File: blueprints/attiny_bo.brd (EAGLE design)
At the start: 35.8 x 20 mm, 8 parts, among them IC1 ATTiny85, J1 AVR_SPI_PRG_6NS

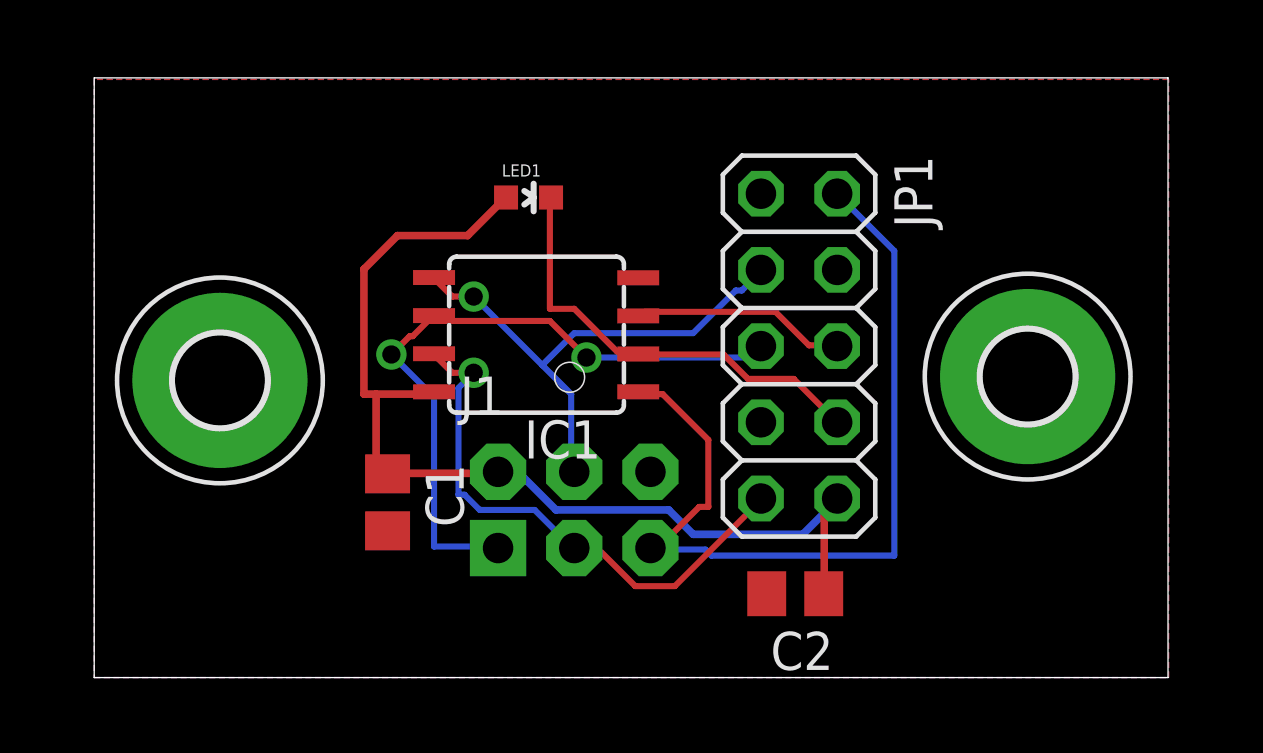
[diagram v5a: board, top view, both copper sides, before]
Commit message: make the board pill-shaped
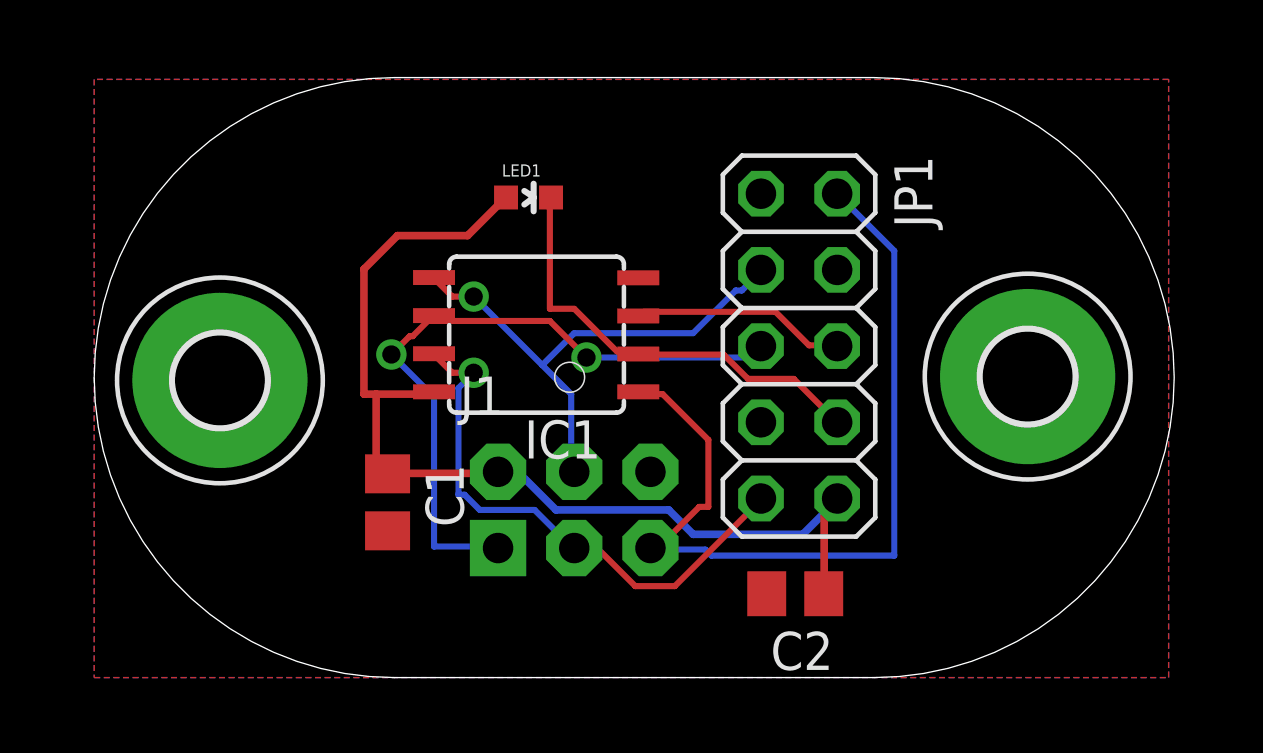
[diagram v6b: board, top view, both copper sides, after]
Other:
- board size 35.8 x 20 mm -> 36 x 20 mm
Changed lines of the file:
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@@
 <setting verticaltext="up"/>
 </settings>
-<grid distance="5" unitdist="mil" unit="mil" style="lines" multiple="1" display="yes" altdistance="5" altunitdist="mm" altunit="mm"/>
+<grid distance="5" unitdist="mil" unit="mm" style="lines" multiple="1" display="yes" altdistance="5" altunitdist="mm" altunit="mm"/>
 <layers>
 <layer number="1" name="Top" color="4" fill="1" visible="yes" active="yes"/>
@@
 <board>
 <plain>
-<wire x1="0" y1="19.99" x2="0" y2="0" width="0" layer="20"/>
-<wire x1="0" y1="0" x2="35.794" y2="0" width="0" layer="20"/>
-<wire x1="35.794" y1="0" x2="35.794" y2="19.99" width="0" layer="20"/>
-<wire x1="35.794" y1="19.99" x2="0" y2="19.99" width="0" layer="20"/>
+<wire x1="10" y1="20" x2="10" y2="0" width="0" layer="20" curve="180"/>
+<wire x1="10" y1="0" x2="26" y2="0" width="0" layer="20"/>
+<wire x1="26" y1="0" x2="26" y2="20" width="0" layer="20" curve="180"/>
+<wire x1="26" y1="20" x2="10" y2="20" width="0" layer="20"/>
 </plain>
 <attributes>

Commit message: making labels
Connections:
- net IN1/MISO renamed PB1
- net N$1 renamed PB4
- net N$3 renamed PB3
- net N$6 renamed PB5
- net SCL/SCK renamed PB2
- net SDA/MOSI renamed PB0
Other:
- board text added: "5V PB3 PB4 GND PB5"
- board text added: "PB2 GND PB1 PB0 GND"
- board text added: "led optional"
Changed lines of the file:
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@@
 <wire x1="26" y1="0" x2="26" y2="20" width="0" layer="20" curve="180"/>
 <wire x1="26" y1="20" x2="10" y2="20" width="0" layer="20"/>
+<text x="27.305" y="4.191" size="0.8128" layer="25" font="vector" rot="R90">5V PB3 PB4 GND PB5</text>
+<text x="20.828" y="4.064" size="0.8128" layer="25" font="vector" rot="R90">PB2 GND PB1 PB0 GND</text>
+<text x="11.811" y="17.145" size="0.6096" layer="25" font="vector">led optional</text>
+<text x="19.939" y="4.064" size="0.8128" layer="26" font="vector" rot="MR90">PB2 GND PB1 PB0 GND</text>
+<text x="26.416" y="4.191" size="0.8128" layer="26" font="vector" rot="MR90">5V PB3 PB4 GND PB5</text>
 </plain>
 <attributes>
@@
 </autorouter>
 <elements>
-<element name="IC1" library="atmel" package="8S2" value="ATTiny85" x="14.732" y="11.43" rot="R90">
+<element name="IC1" library="atmel" package="8S2" value="ATTiny85" x="14.732" y="11.43" smashed="yes" rot="R90">
 <attribute name="OC_NEWARK" value="96K6522" x="19.812" y="38.1" size="1.778" layer="27" rot="R90" display="off"/>
 <attribute name="MPN" value="ATTINY13-20SU" x="19.812" y="38.1" size="1.778" layer="27" rot="R90" display="off"/>
@@
 <attribute name="OC_FARNELL" value="9171568" x="19.812" y="38.1" size="1.778" layer="27" rot="R90" display="off"/>
 </element>
-<element name="J1" library="SparkFun-Connectors" package="2X3-NS" value="AVR_SPI_PRG_6NS" x="16.002" y="5.588"/>
-<element name="C1" library="rcl" package="C0805" value="" x="9.779" y="5.842" rot="R270"/>
-<element name="LED1" library="SparkFun-LED" package="LED-0603" value="" x="14.478" y="16.002" rot="R270"/>
-<element name="JP1" library="pinhead" package="2X05" value="" x="23.495" y="11.049" rot="R270"/>
-<element name="C2" library="rcl" package="C0805" value="" x="23.368" y="2.794" rot="R180"/>
-<element name="H1" library="holes" package="3,0-PAD" value="MOUNT-PAD-ROUND3.0" x="4.191" y="9.906"/>
-<element name="H2" library="holes" package="3,0-PAD" value="MOUNT-PAD-ROUND3.0" x="31.115" y="10.033"/>
+<element name="J1" library="SparkFun-Connectors" package="2X3-NS" value="AVR_SPI_PRG_6NS" x="16.002" y="5.588" smashed="yes"/>
+<element name="C1" library="rcl" package="C0805" value="" x="9.779" y="5.842" smashed="yes" rot="R270">
+<attribute name="VALUE" x="7.239" y="7.112" size="1.27" layer="27" rot="R270"/>
+</element>
+<element name="LED1" library="SparkFun-LED" package="LED-0603" value="" x="14.478" y="16.002" smashed="yes" rot="R270">
+<attribute name="VALUE" x="13.462" y="14.9225" size="0.4064" layer="27"/>
+</element>
+<element name="JP1" library="pinhead" package="2X05" value="" x="23.495" y="11.049" smashed="yes" rot="R270">
+<attribute name="VALUE" x="19.05" y="17.399" size="1.27" layer="27" rot="R270"/>
+</element>
+<element name="C2" library="rcl" package="C0805" value="" x="23.368" y="2.794" smashed="yes" rot="R180">
+<attribute name="VALUE" x="24.638" y="5.334" size="1.27" layer="27" rot="R180"/>
+</element>
+<element name="H1" library="holes" package="3,0-PAD" value="MOUNT-PAD-ROUND3.0" x="4.191" y="9.906" smashed="yes"/>
+<element name="H2" library="holes" package="3,0-PAD" value="MOUNT-PAD-ROUND3.0" x="31.115" y="10.033" smashed="yes"/>
 </elements>
 <signals>
-<signal name="IN1/MISO">
+<signal name="PB1">
 <contactref element="IC1" pad="6"/>
 <contactref element="J1" pad="1"/>
@@
 <wire x1="9.8044" y1="6.9088" x2="9.779" y2="6.792" width="0.254" layer="1"/>
 </signal>
-<signal name="SDA/MOSI">
+<signal name="PB0">
 <contactref element="IC1" pad="5"/>
 <contactref element="J1" pad="4"/>
@@
 <via x="12.6492" y="12.7" extent="1-16" drill="0.6096"/>
 </signal>
-<signal name="N$6">
+<signal name="PB5">
 <contactref element="IC1" pad="1"/>
 <contactref element="J1" pad="5"/>
@@
 <wire x1="18.542" y1="4.2672" x2="18.542" y2="4.318" width="0.2032" layer="16"/>
 </signal>
-<signal name="SCL/SCK">
+<signal name="PB2">
 <contactref element="IC1" pad="7"/>
 <contactref element="J1" pad="3"/>
@@
 <via x="12.6492" y="10.16" extent="1-16" drill="0.6096"/>
 </signal>
-<signal name="N$3">
+<signal name="PB3">
 <contactref element="LED1" pad="C"/>
 <contactref element="IC1" pad="2"/>
@@
 <wire x1="18.2372" y1="10.7696" x2="18.136" y2="10.785" width="0.2032" layer="1"/>
 </signal>
-<signal name="N$1">
+<signal name="PB4">
 <contactref element="IC1" pad="3"/>
 <contactref element="JP1" pad="6"/>
